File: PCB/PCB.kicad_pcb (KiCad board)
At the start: 4 copper layers, 75 x 75 mm, 149 parts, among them J1 Conn_01x06_Female, J2 5054332681

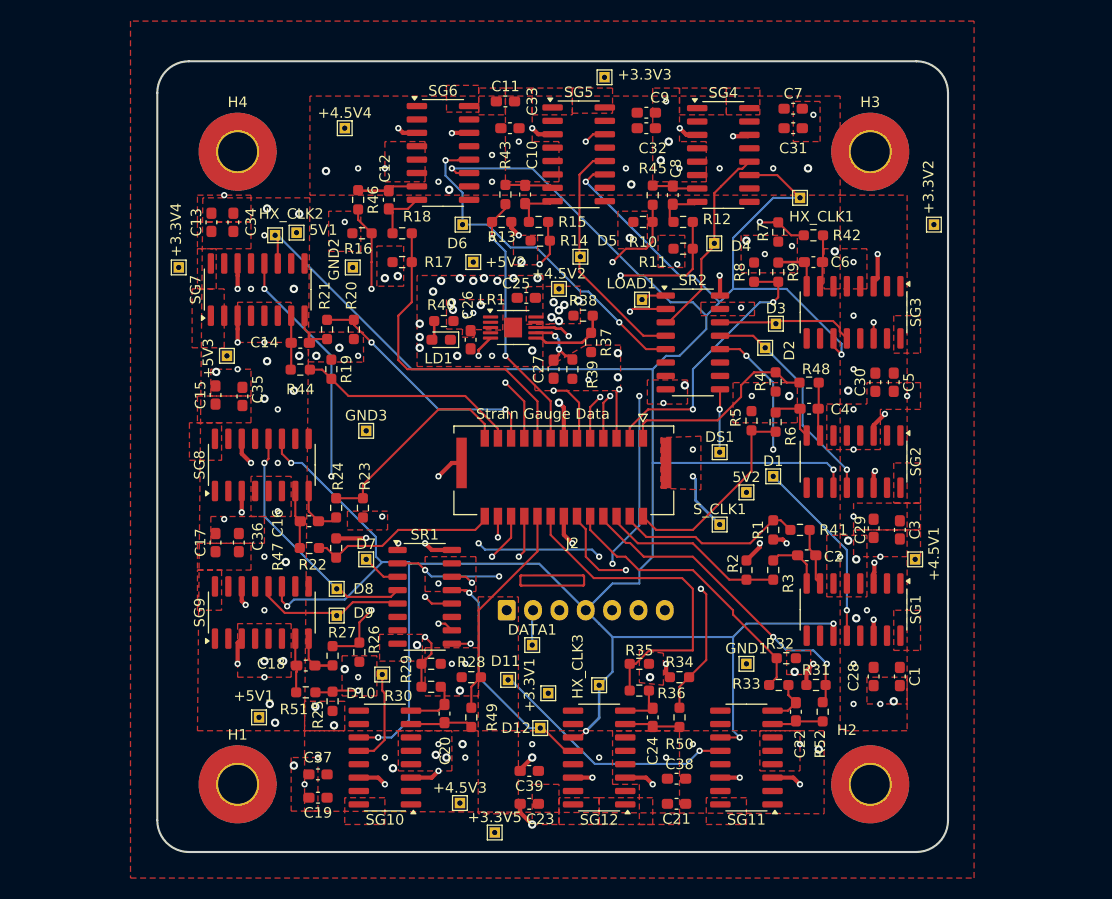
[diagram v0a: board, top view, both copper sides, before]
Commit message: Silkscreen updated
The strain gauges are correctly labeled now as well as the test points for all individual hx711 amplifiers. All the voltages are completely labeled as well. There are many 4.5V, 5V and 3.3V  test points. Every digital signal has its test point. To place the test points, I replaced some of the vias with test points or spliced two lines together.
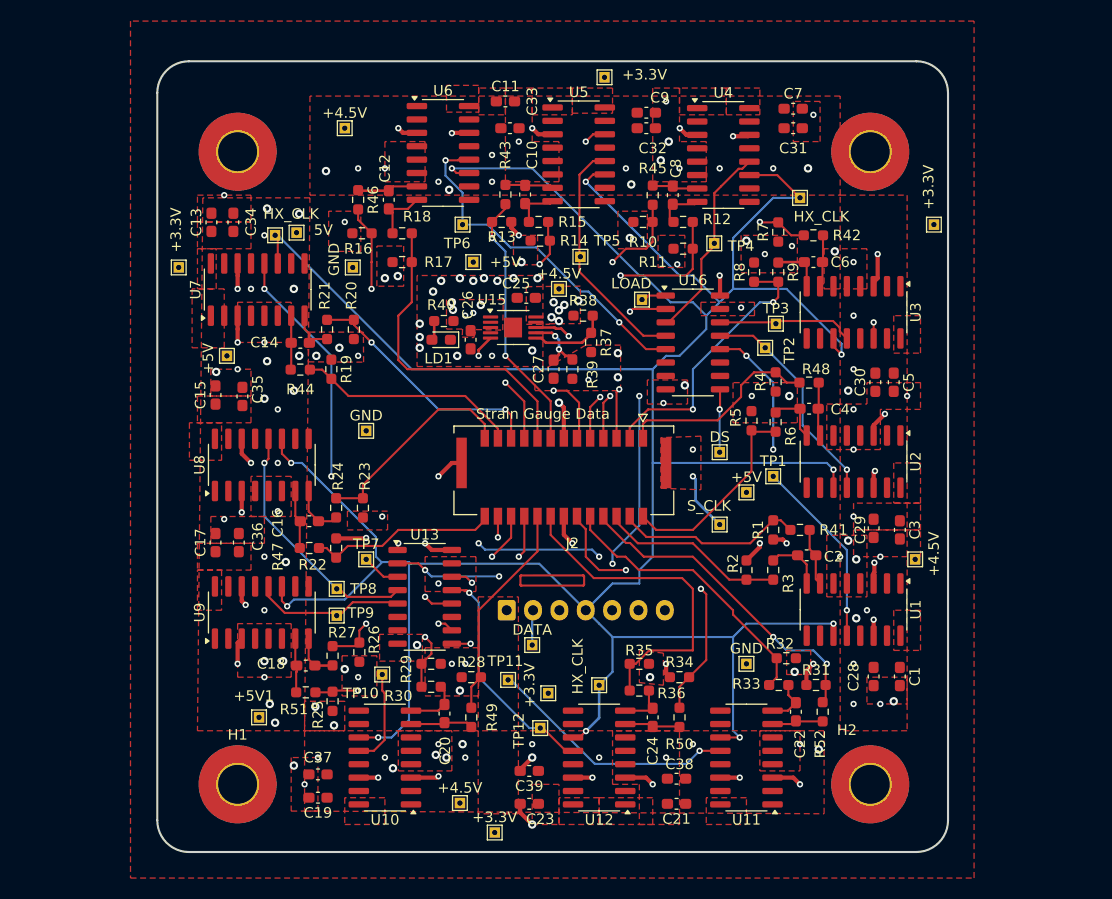
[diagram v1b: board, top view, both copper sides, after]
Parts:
- renumbered +3.3V5 to +3.3V, +3.3V2 to +3.3V, +3.3V1 to +3.3V, +3.3V4 to +3.3V, +3.3V3 to +3.3V, +4.5V3 to +4.5V, +4.5V1 to +4.5V, +4.5V4 to +4.5V, +4.5V2 to +4.5V, 5V2 to +5V, +5V2 to +5V, +5V3 to +5V, 5V1 to 5V, DATA1 to DATA, DS1 to DS, GND3 to GND, GND2 to GND, GND1 to GND, HX_CLK3 to HX_CLK, HX_CLK2 to HX_CLK, HX_CLK1 to HX_CLK, LOAD1 to LOAD, S_CLK1 to S_CLK, D1 to TP1, D10 to TP10, D11 to TP11, D12 to TP12, D2 to TP2, D3 to TP3, D4 to TP4, D5 to TP5, D6 to TP6, D7 to TP7, D8 to TP8, D9 to TP9, SG1 to U1, SG10 to U10, SG11 to U11, SG12 to U12, SR1 to U13, LR1 to U15, SR2 to U16, SG2 to U2, SG3 to U3, SG4 to U4, SG5 to U5, SG6 to U6, SG7 to U7, SG8 to U8, SG9 to U9
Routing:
- net GND: track 48.4 -> 47.5 mm

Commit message: Updated Linear Regulator Layout
Linear regulator layout has been updated to better match the data sheet and the labels for every test point have been cleaned up.
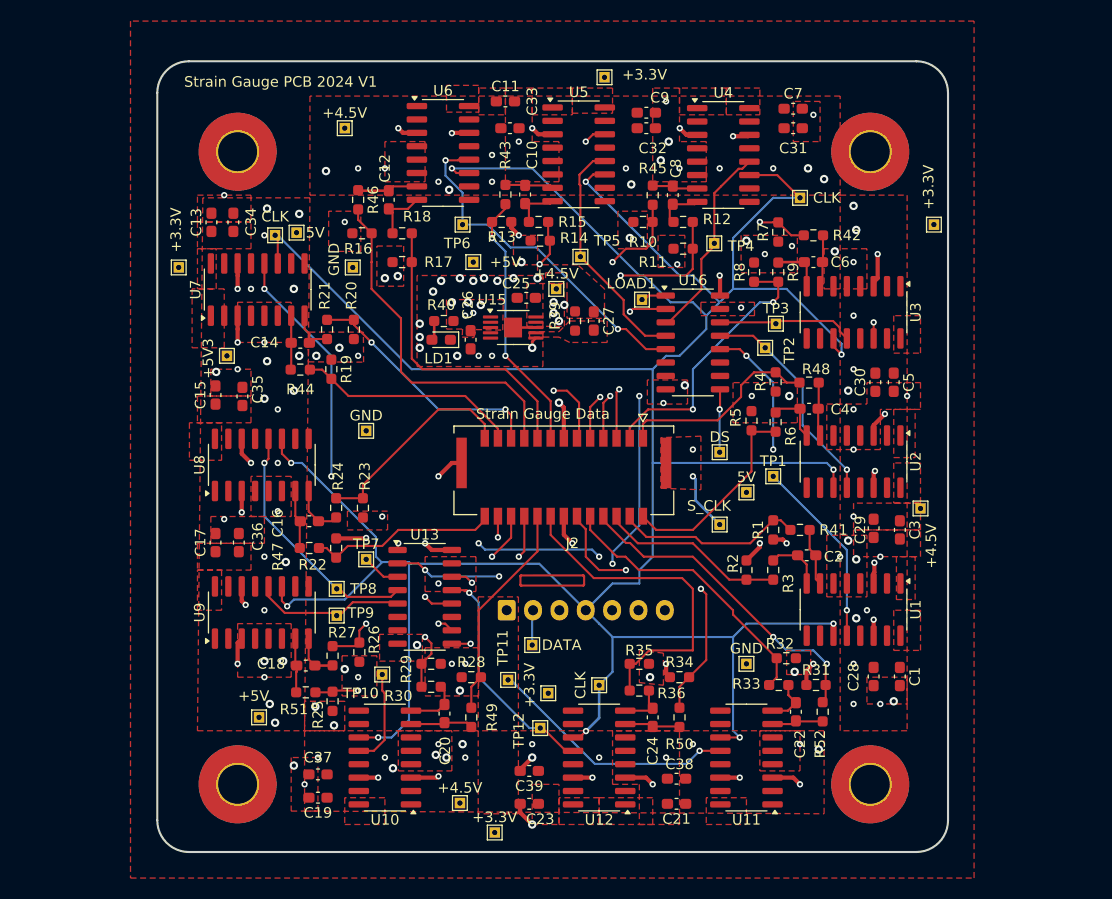
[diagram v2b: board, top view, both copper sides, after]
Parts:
- removed R37: 49.9K, Resistor_SMD:R_0603_1608Metric_Pad0.98x0.95mm_HandSolder
- removed R38: 453K, Resistor_SMD:R_0603_1608Metric_Pad0.98x0.95mm_HandSolder
- added G***: LOGO, Symbols:Martlet 2, B.Cu at (244.6, 123.7)
- moved C27 5.95 mm to (249.7, 108.5), turned to -90 degrees
- moved +4.5V 4.85 mm to (280.7, 126.2)
- moved R39 4.58 mm to (247.9, 108.5), turned to -90 degrees
- moved +4.5V 0.25 mm to (246.1, 105.4)
- renumbered +5V1 to +5V, +5V to +5V3, +5V to 5V, HX_CLK to CLK, LOAD to LOAD1
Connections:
- net Net-(U15-SET) renamed /SET
- U15 pad 6: Net-(U15-PGFB) -> +5V
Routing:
- net +5V: track 4.72 -> 13.9 mm, vias 52 -> 56
- net Net-(U15-PGFB): track 7.34 -> 0.00 mm
- net /SET: track 6.90 -> 0.00 mm, vias 2 -> 0
- net GND: track 47.5 -> 44.0 mm, vias 103 -> 98
- net /H10N: track 30.9 -> 29.0 mm
- net 4.5V: vias 20 -> 18
- net /H10P: vias 2 -> 0
- added copper zone on F.Cu, net /SET
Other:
- board text added: "Alex Thornewell"
- board text added: "Strain Gauge PCB 2024 V1"

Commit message: Fixed linear regulator
Linear regulator has been set up to Mateo's proportions. Test points have also been moved.
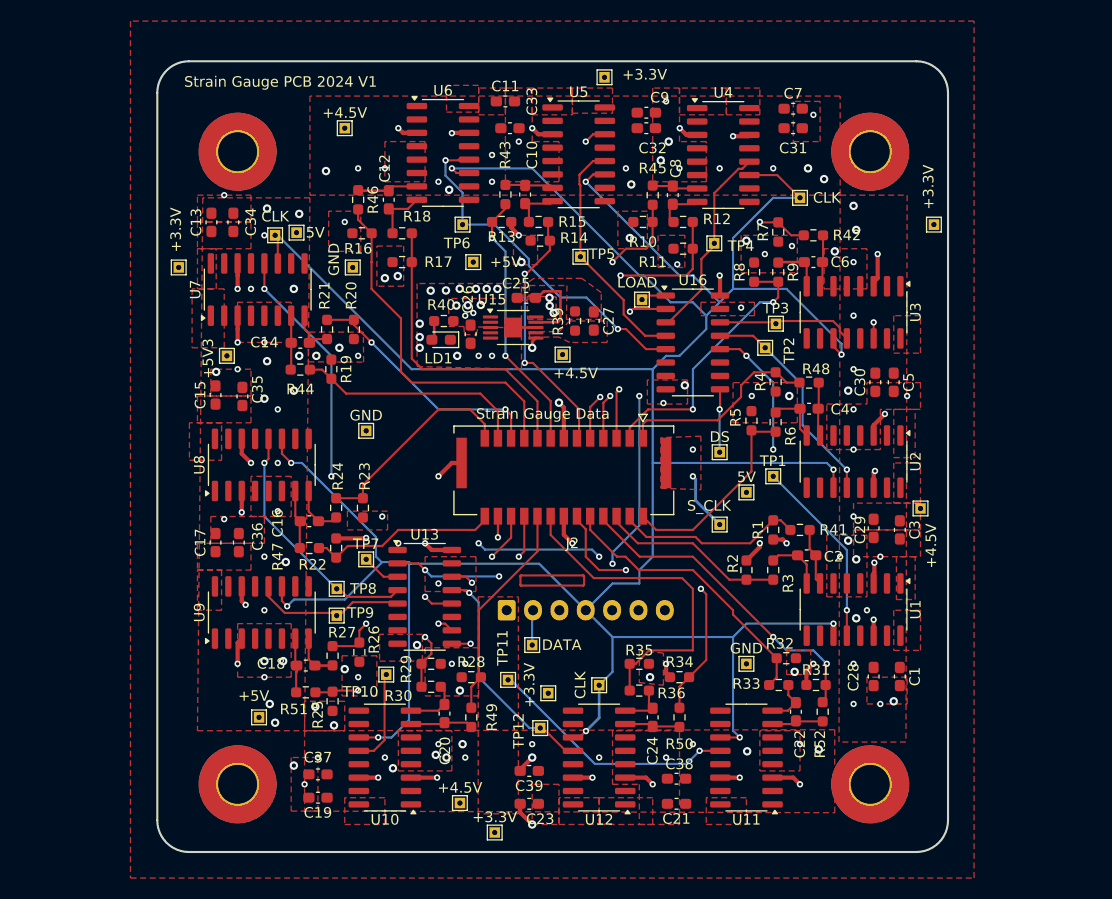
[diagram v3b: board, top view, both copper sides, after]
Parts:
- moved +4.5V 6.26 mm to (246.7, 111.6)
- moved C26 0.53 mm to (238.0, 109.7)
- moved TP10 0.38 mm to (230.0, 142.0)
- renumbered LOAD1 to LOAD
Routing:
- net 4.5V: track 35.7 -> 43.3 mm, vias 18 -> 17
- net /H3P: track 21.1 -> 22.0 mm
- net /H2N: track 25.0 -> 24.5 mm
- net GND: vias 98 -> 96
- net +5V: vias 56 -> 57

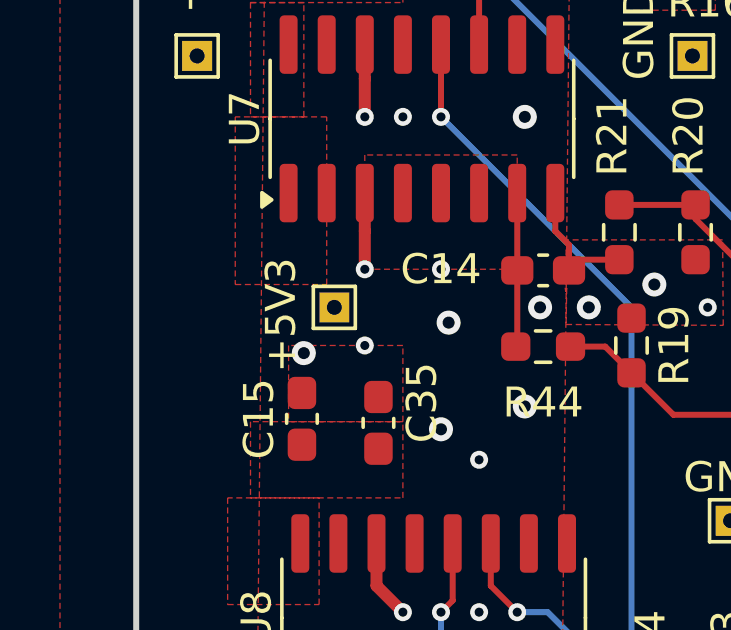
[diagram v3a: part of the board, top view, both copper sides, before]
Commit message: Fixed silkscreen
Silkscreen updated to better suit everything as a label was not corrected earlier.
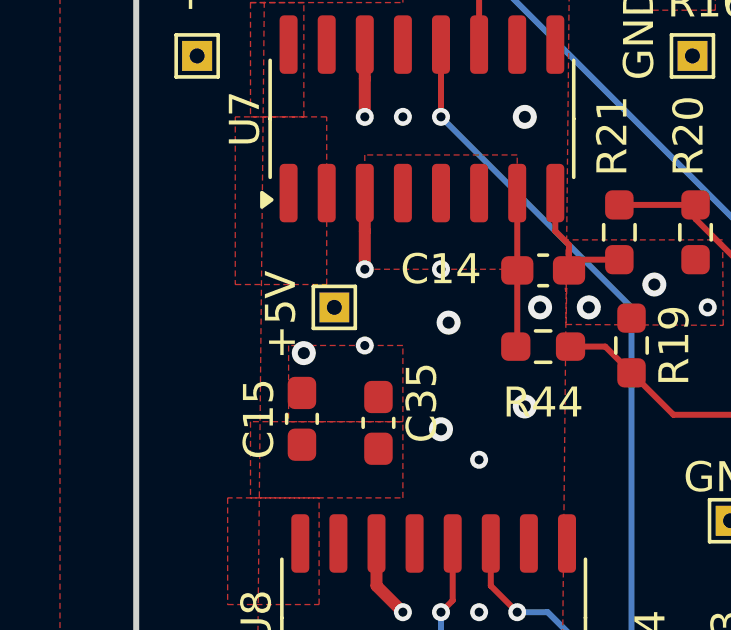
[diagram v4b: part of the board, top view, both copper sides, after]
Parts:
- renumbered +5V3 to +5V
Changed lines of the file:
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@@
 		(tags "test point THT pad rectangle square")
 		(property "Reference" "+4.5V"
-			(at 1.016 3.556 270)
+			(at 1.016 3.556 -90)
 			(layer "F.SilkS")
 			(effects
@@
 		(tags "test point THT pad rectangle square")
 		(property "Reference" "+3.3V"
-			(at -0.508 -3.556 270)
+			(at -0.508 -3.556 -90)
 			(layer "F.SilkS")
 			(effects
@@
 		(tags "test point THT pad rectangle square")
 		(property "Reference" "CLK"
-			(at -1.778 0 270)
+			(at -1.778 0 -90)
 			(layer "F.SilkS")
 			(effects
@@
 		(descr "THT rectangular pad as test Point, square 1.0mm side length, hole diameter 0.5mm")
 		(tags "test point THT pad rectangle square")
-		(property "Reference" "+5V3"
+		(property "Reference" "+5V"
 			(at -1.778 0.254 90)
 			(layer "F.SilkS")

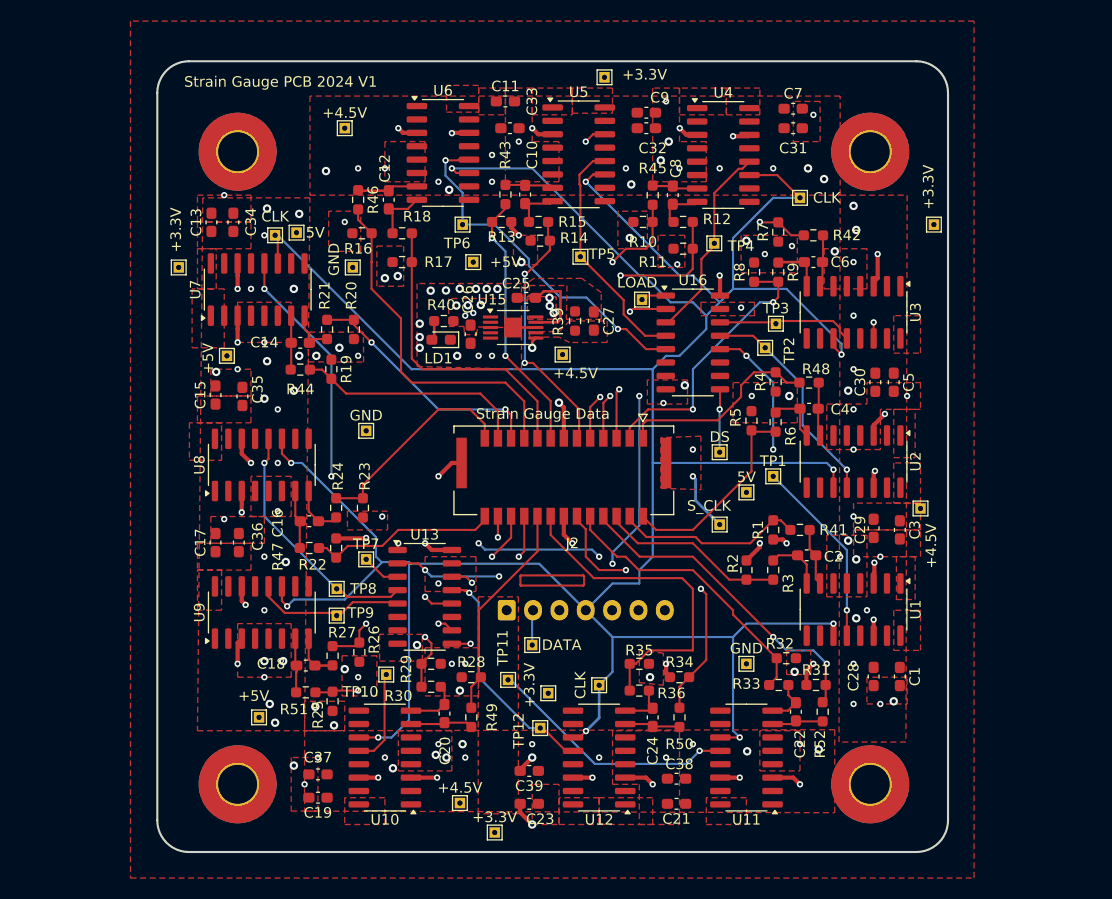
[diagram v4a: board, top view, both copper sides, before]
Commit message: Post review first draft
Taking into account many of the pieces of feedback received in the pcb review on Wednesday by changing the locations of the shift registers and rewiring accordingly.
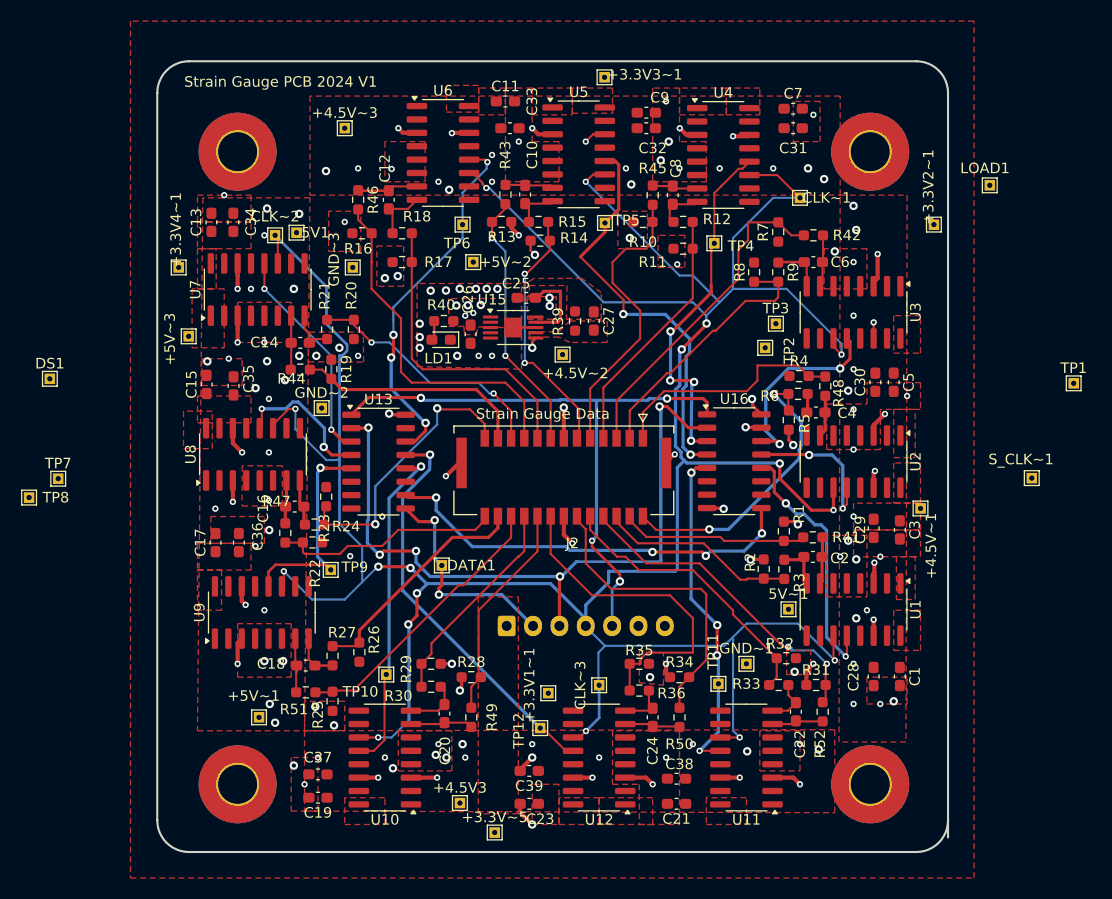
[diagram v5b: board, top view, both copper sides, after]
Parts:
- moved DS1 63.9 mm to (198.1, 113.9)
- moved LOAD1 34.7 mm to (287.2, 95.6)
- moved TP8 30.4 mm to (196.1, 125.2)
- moved TP7 30.2 mm to (198.9, 123.4)
- moved S_CLK~1 29.9 mm to (291.2, 123.4)
- moved TP1 29.8 mm to (295.2, 114.4)
- moved TP11 19.9 mm to (261.5, 142.9)
- moved U13 13.6 mm to (229.3, 121.8)
- moved U16 11.9 mm to (263.0, 121.8)
- moved 5V~1 11.8 mm to (268.1, 135.8)
- moved DATA1 11.4 mm to (235.3, 131.6)
- moved GND~2 4.74 mm to (223.9, 116.7)
- moved TP9 4.38 mm to (224.7, 132.1)
- moved +5V~3 4.07 mm to (211.3, 109.9)
- moved TP5 3.96 mm to (250.7, 99.2)
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- renumbered +3.3V to +3.3V1~1, +3.3V to +3.3V2~1, +3.3V to +3.3V3~1, +3.3V to +3.3V4~1, +3.3V to +3.3V~5, +4.5V to +4.5V3, +4.5V to +4.5V~1, +4.5V to +4.5V~2, +4.5V to +4.5V~3, +5V to +5V~1, +5V to +5V~2, +5V to +5V~3, 5V to 5V1, 5V to 5V~1, CLK to CLK~1, CLK to CLK~2, CLK to CLK~3, DATA to DATA1, DS to DS1, GND to GND~1, GND to GND~2, GND to GND~3, LOAD to LOAD1, S_CLK to S_CLK~1
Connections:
- U13 pad 14: /DOUT5 -> /DOUT10
- U16 pad 5: /DOUT10 -> /DOUT5
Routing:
- net /DOUT14: track 22.0 -> 38.8 mm
- net /DOUT2: track 22.8 -> 39.3 mm, vias 0 -> 2
- net /DOUT9: track 18.6 -> 33.9 mm, vias 0 -> 4
- net /DOUT3: track 35.9 -> 20.8 mm
- net /DOUT13: track 20.8 -> 31.8 mm
- net /DATA: track 10.9 -> 21.7 mm, vias 1 -> 2
- net /H12N: track 19.4 -> 30.2 mm, vias 0 -> 2
- net /DOUT11: track 23.8 -> 14.0 mm, vias 1 -> 2
- net /DOUT: track 33.3 -> 24.5 mm, vias 3 -> 2
- net /DOUT4: track 14.5 -> 21.9 mm, vias 0 -> 1
- net /DOUT12: track 21.2 -> 14.4 mm, vias 1 -> 2
- net /H11N: track 20.2 -> 27.1 mm, vias 0 -> 2
- net Net-(U13-DS): track 47.0 -> 40.3 mm
- net /DOUT1: track 13.5 -> 19.7 mm, vias 0 -> 2
- net HX_CLK: track 306.8 -> 300.6 mm, vias 10 -> 17
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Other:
- outline, holes or cut-outs redrawn
